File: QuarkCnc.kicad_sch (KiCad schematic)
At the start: 35 parts, among them J1 Conn_02x03_Counter_Clockwise, J10 Screw_Terminal_01x02, J11 Screw_Terminal_01x02, J12 Screw_Terminal_01x02, J13 Screw_Terminal_01x03, J14 Screw_Terminal_01x03, J15 Screw_Terminal_01x03, J16 Screw_Terminal_01x03, J17 Screw_Terminal_01x03, J18 Screw_Terminal_01x05, J19 Screw_Terminal_01x04, J2 Conn_02x03_Counter_Clockwise, J20 Screw_Terminal_01x04, J21 Screw_Terminal_01x04, J22 Screw_Terminal_01x04, J23 Screw_Terminal_01x04, J24 Screw_Terminal_01x06, J25 Screw_Terminal_01x06, J26 Screw_Terminal_01x06, J27 Screw_Terminal_01x06, J28 Screw_Terminal_01x06, J3 USB_B_Micro, J4 Screw_Terminal_01x02, J5 Screw_Terminal_01x03, J6 Conn_01x03_Male, J7 Screw_Terminal_01x02, J8 Screw_Terminal_01x02, J9 Screw_Terminal_01x02, U1 1455U2801, U2 LRS-350-48, U3 RSP-500-48

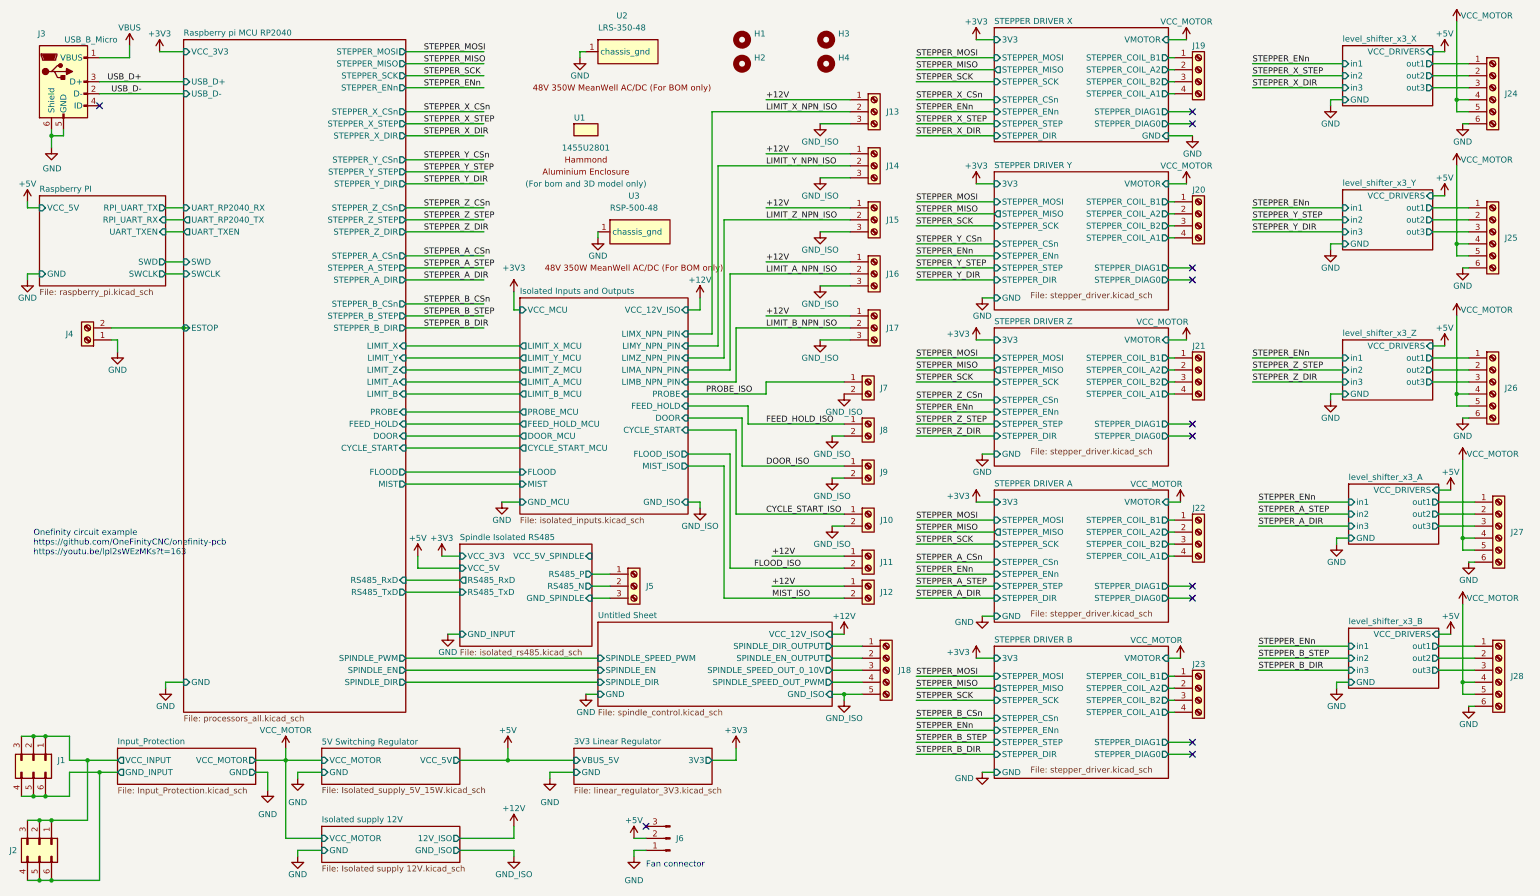
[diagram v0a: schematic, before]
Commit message: Refactored top sheet
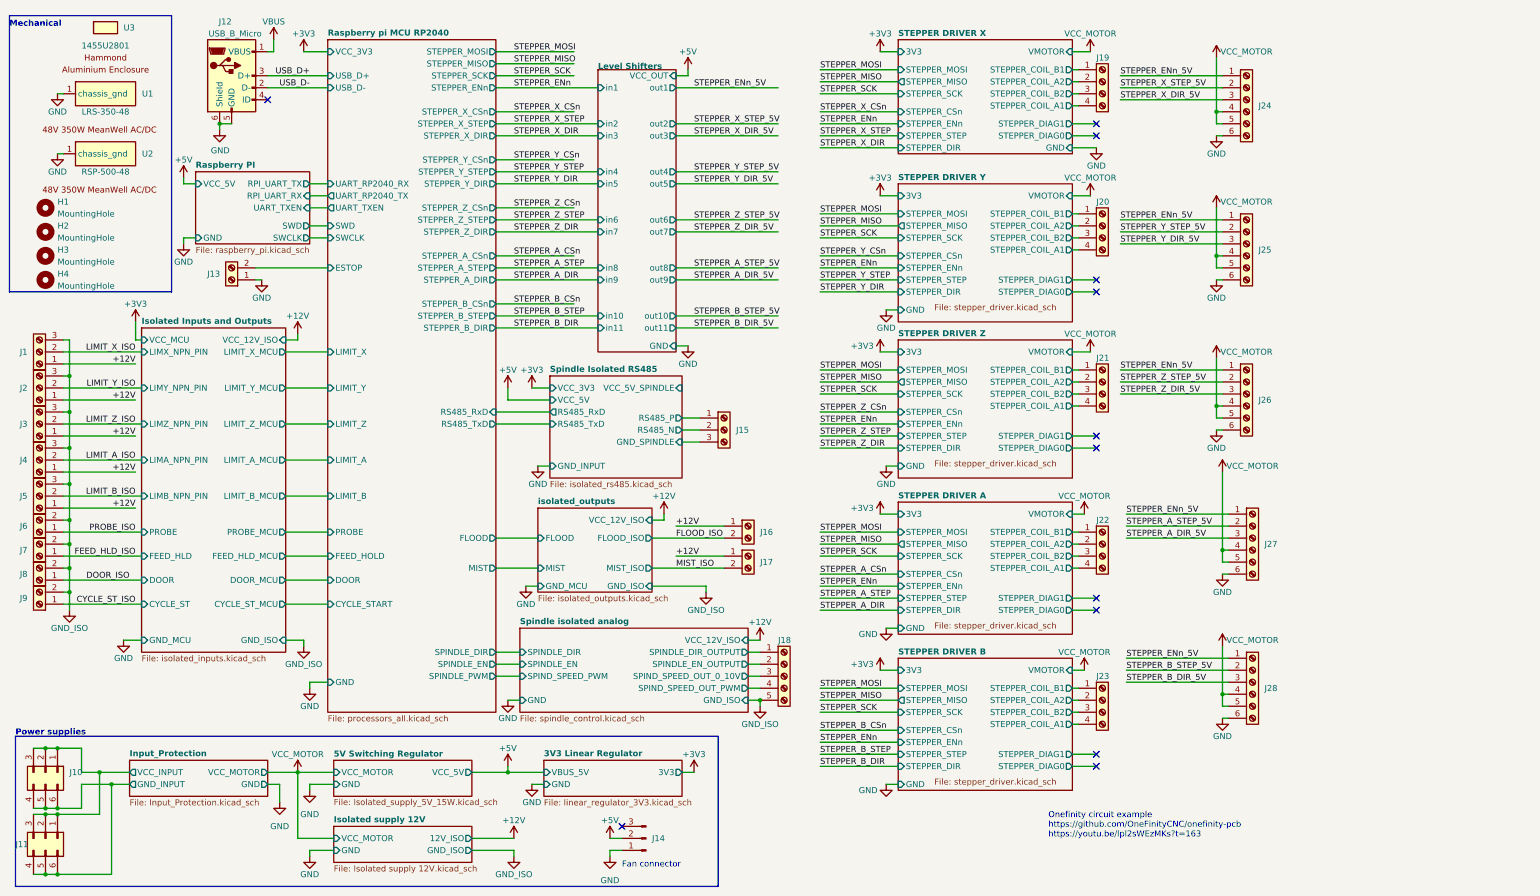
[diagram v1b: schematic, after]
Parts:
- H1, H2, H3, H4: value (none) -> MountingHole; footprint (none) -> MountingHole:MountingHole_4.3mm_M4_ISO7380
- U3: renamed from U1; Comment (For bom and 3D model only) -> (none)
- renumbered J13 to J1, J1 to J10, J2 to J11, J3 to J12, J4 to J13, J6 to J14, J5 to J15, J11 to J16, J12 to J17, J14 to J2, J15 to J3, J16 to J4, J17 to J5, J7 to J6, J8 to J7, J9 to J8, J10 to J9, U2 to U1, U3 to U2
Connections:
- net level_shifter_x3_B/out1 is gone; now on net STEPPER_ENn_5V: J28.1 (Pin_1)
- net level_shifter_x3_X/out1 is gone; now on net STEPPER_ENn_5V: J24.1 (Pin_1)
- net level_shifter_x3_Y/out1 is gone; now on net STEPPER_ENn_5V: J25.1 (Pin_1)
- net level_shifter_x3_Z/out1 is gone; now on net STEPPER_ENn_5V: J26.1 (Pin_1)
- net CYCLE_START_ISO renamed CYCLE_ST_ISO
- net FEED_HOLD_ISO renamed FEED_HLD_ISO
- net LIMIT_A_NPN_ISO renamed LIMIT_A_ISO
- net LIMIT_B_NPN_ISO renamed LIMIT_B_ISO
- net LIMIT_X_NPN_ISO renamed LIMIT_X_ISO
- net LIMIT_Y_NPN_ISO renamed LIMIT_Y_ISO
- net LIMIT_Z_NPN_ISO renamed LIMIT_Z_ISO
- net Spindle isolated analog/SPINDLE_SPEED_OUT_0_10V renamed Spindle isolated analog/SPIND_SPEED_OUT_0_10V
- net Spindle isolated analog/SPINDLE_SPEED_OUT_PWM renamed Spindle isolated analog/SPIND_SPEED_OUT_PWM
- net level_shifter_x3_A/out1 renamed STEPPER_ENn_5V
- net level_shifter_x3_A/out2 renamed STEPPER_A_STEP_5V
- net level_shifter_x3_A/out3 renamed STEPPER_A_DIR_5V
- net level_shifter_x3_B/out2 renamed STEPPER_B_STEP_5V
- net level_shifter_x3_B/out3 renamed STEPPER_B_DIR_5V
- net level_shifter_x3_X/out2 renamed STEPPER_X_STEP_5V
- net level_shifter_x3_X/out3 renamed STEPPER_X_DIR_5V
- net level_shifter_x3_Y/out2 renamed STEPPER_Y_STEP_5V
- net level_shifter_x3_Y/out3 renamed STEPPER_Y_DIR_5V
- net level_shifter_x3_Z/out2 renamed STEPPER_Z_STEP_5V
- net level_shifter_x3_Z/out3 renamed STEPPER_Z_DIR_5V
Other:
- sheet Untitled Sheet renamed Spindle isolated analog
- removed sheet level_shifter_x3_A
- removed sheet level_shifter_x3_B
- removed sheet level_shifter_x3_X
- removed sheet level_shifter_x3_Y
- removed sheet level_shifter_x3_Z
- added sheet Level Shifters (level_shifter_x3.kicad_sch)
- added sheet isolated_outputs (isolated_outputs.kicad_sch)
- sheet Isolated Inputs and Outputs ports: added CYCLE_ST, CYCLE_ST_MCU, FEED_HLD, FEED_HLD_MCU; removed CYCLE_START, CYCLE_START_MCU, FEED_HOLD, FEED_HOLD_MCU, FLOOD, FLOOD_ISO, MIST, MIST_ISO
- sheet Spindle isolated analog ports: added SPIND_SPEED_OUT_0_10V, SPIND_SPEED_OUT_PWM, SPIND_SPEED_PWM; removed SPINDLE_SPEED_OUT_0_10V, SPINDLE_SPEED_OUT_PWM, SPINDLE_SPEED_PWM
- note added: "Mechanical"
- note added: "Power supplies"
- moved on the sheet: H1, H2, H3, H4, J1, J10, J11, J12, J13, J14, J15, J16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
